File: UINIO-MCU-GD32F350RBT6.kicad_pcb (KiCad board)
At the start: 2 copper layers, 88.1 x 20.3 mm, 39 parts, among them J1 Conn_01x32_Pin, J2 Conn_01x32_Pin, J3 Conn_01x04_Pin, SW1 BOOT0, SW2 NRST, U1 ME6211C33M5G-N, U2 GD32F350RBT6, Y1 32.768KHz, Y2 8MHz

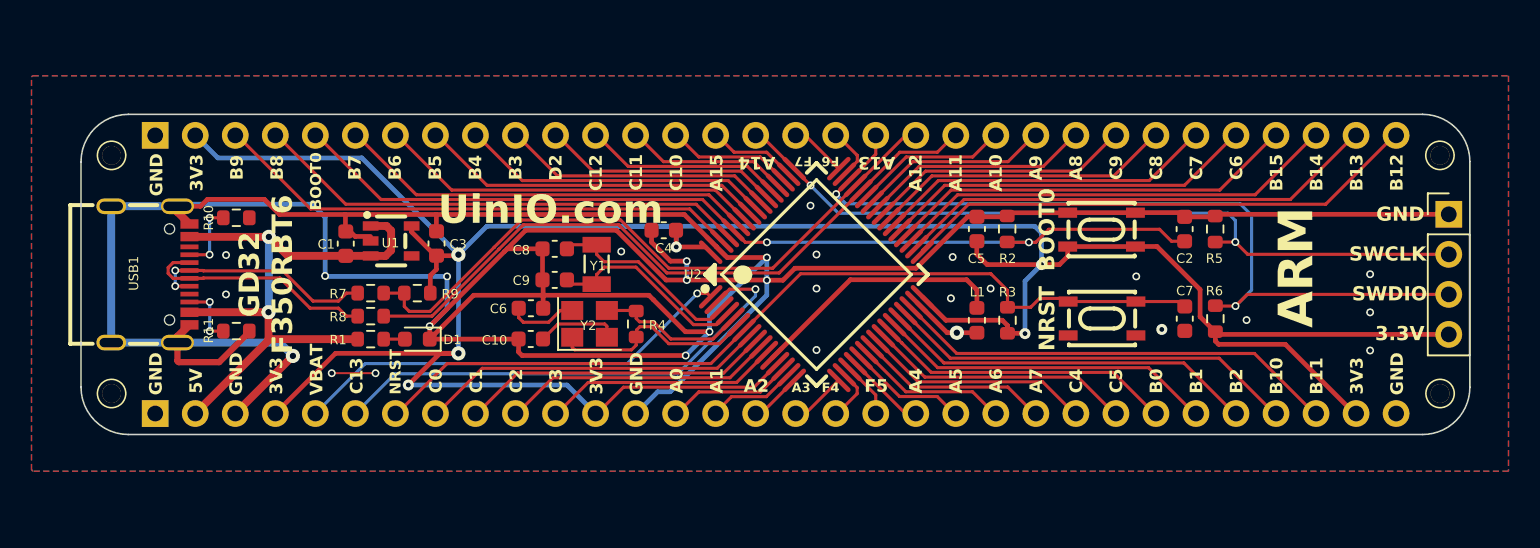
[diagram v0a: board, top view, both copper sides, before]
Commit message: Release UINIO-MCU-GD32F350RBT6 version 3.0.1.
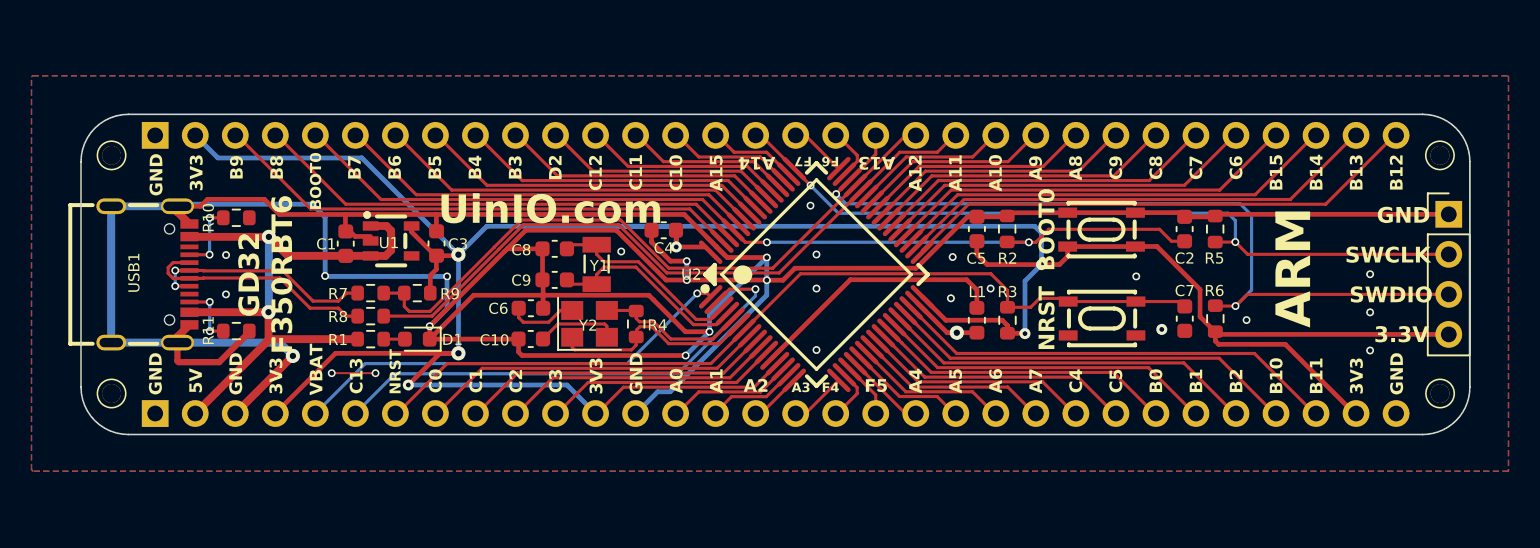
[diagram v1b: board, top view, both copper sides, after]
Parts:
- removed ? (x2): LOGO, LOGO
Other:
- board text added: "Version 3.0.1"
- board text removed: "Version 3.0.0"

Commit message: Release UINIO-MCU-GD32F350RBT6 version 3.1.1.
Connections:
- R1 pad 2: /VDD_5V -> /VDD_3.3V
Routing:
- net /VDD_5V: track 40.0 -> 34.3 mm
- net /VDD_3.3V: track 184.7 -> 185.6 mm
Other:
- board text added: "Version 3.1.1"
- board text removed: "Version 3.0.1"

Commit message: Release UINIO-MCU-GD32F350RBT6 version 3.2.0.
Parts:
- removed R4: 1M, Resistor_SMD:R_0603_1608Metric
- removed R9: 1.5K, Resistor_SMD:R_0603_1608Metric
- added C11: 0.1uF, Capacitor_SMD:C_0603_1608Metric, F.Cu at (143.5, 105.6)
- moved R10 9.66 mm to (125.5, 102.8)
- moved R11 9.25 mm to (125.5, 107.2)
- moved C6 3.23 mm to (134.9, 109.0), turned to 0 degrees
- moved C3 2.53 mm to (128.9, 99.1), turned to 90 degrees
- moved J1 2.53 mm to (111.1, 115.0)
- moved J2 2.53 mm to (111.1, 92.3)
- moved C1 2.18 mm to (123.2, 99.5)
- moved U1 2.18 mm to (126.1, 99.3)
- moved C8 2.17 mm to (134.9, 100.4)
- moved Y1 2.10 mm to (137.6, 101.5)
- moved C9 2.01 mm to (134.9, 102.7)
- moved Y2 1.27 mm to (138.1, 107.9), turned to 90 degrees
- moved R1 1.18 mm to (125.5, 108.7)
- moved C10 0.92 mm to (134.9, 106.8)
- moved R8 0.90 mm to (125.5, 105.8)
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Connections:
- L1 pad 1: GND -> /VDD_3.3V
- L1 pad 2: /VSSA -> Net-(U2-VDDA)
- U2 pad 12: /VSSA -> GND
- U2 pad 13: /VDD_3.3V -> Net-(U2-VDDA)
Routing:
- net GND: track 254.8 -> 129.0 mm, vias 29 -> 48
- net /VDD_3.3V: track 185.6 -> 166.4 mm
- net /VSSA: track 16.5 -> 0.00 mm
- net Net-(U2-VDDA): track 0.00 -> 16.1 mm
- net Net-(USB1-CC2): track 4.00 -> 12.1 mm, vias 2 -> 0
- net Net-(USB1-CC1): track 4.49 -> 11.6 mm, vias 2 -> 0
- net /VBAT: track 28.3 -> 33.2 mm
- net /PA12: track 41.4 -> 45.2 mm
- net /PF1: track 13.3 -> 10.1 mm
- net Net-(U2-PC14-OSC32IN): track 12.2 -> 15.4 mm
- net Net-(U2-PC15-OSC32OUT): track 12.5 -> 15.7 mm
- net /PA11: track 43.6 -> 46.7 mm
- net Net-(C6-Pad2): track 4.42 -> 1.54 mm
- net /PA4: track 4.47 -> 7.28 mm
- net /PA2: track 2.97 -> 5.64 mm
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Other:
- board size 88.1 x 20.3 mm -> 88.1 x 25.4 mm
- board text added: "Version 3.2.0"
- board text removed: "ARM"
- board text removed: "Version 3.1.1"
